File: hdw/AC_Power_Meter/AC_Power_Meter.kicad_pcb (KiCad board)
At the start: 4 copper layers, 100 x 100 mm, 280 parts, among them J1001 USB_B_Mini, J1701 Ext_SW_Toggle, J201 HT_IN, J202 NEUT_IN, J203 EARTH_IN, J401 HT_OUT, J402 NEUT_OUT, J403 EARTH_OUT, J501 AUX_IN, J801 Prog, Q1501 BT139-600, Q501 DMP3099L-7, SW1702 MRESET, SW1703 SW_Toggle, U1001 LT6700-1-S6, U1002 FT234XD, U1003 74LVC1G06, U1004 TPD3S014DBVR, U1101 ISO7321C, U1201 SSD1306, U1401 LTV-356T, U1402 74LVC1G17, U1501 74LVC1G32, U1502 FOD4218, U1601 74LVC1G06, U1602 74LVC1G06, U1603 74LVC1G06, U1604 74LVC1G06, U1605 74LVC1G06, U1606 74LVC1G06, U1607 74LVC1G06, U1702 TLC555CPS, U301 ACS722LLCTR-20AB, U501 LT6700-1-S6, U502 74LVC1G17, U601 74LVC1G17, U602 LT3973-DD, U701 PIC18LF67K40-I/PT, U801 TL331, U802 74LVC1G86, U901 LTC6240IS5, U902 LTC6240IS5, U903 LTC6240IS5, U904 LTC6240IS5, X701 ASV-16.000MHz

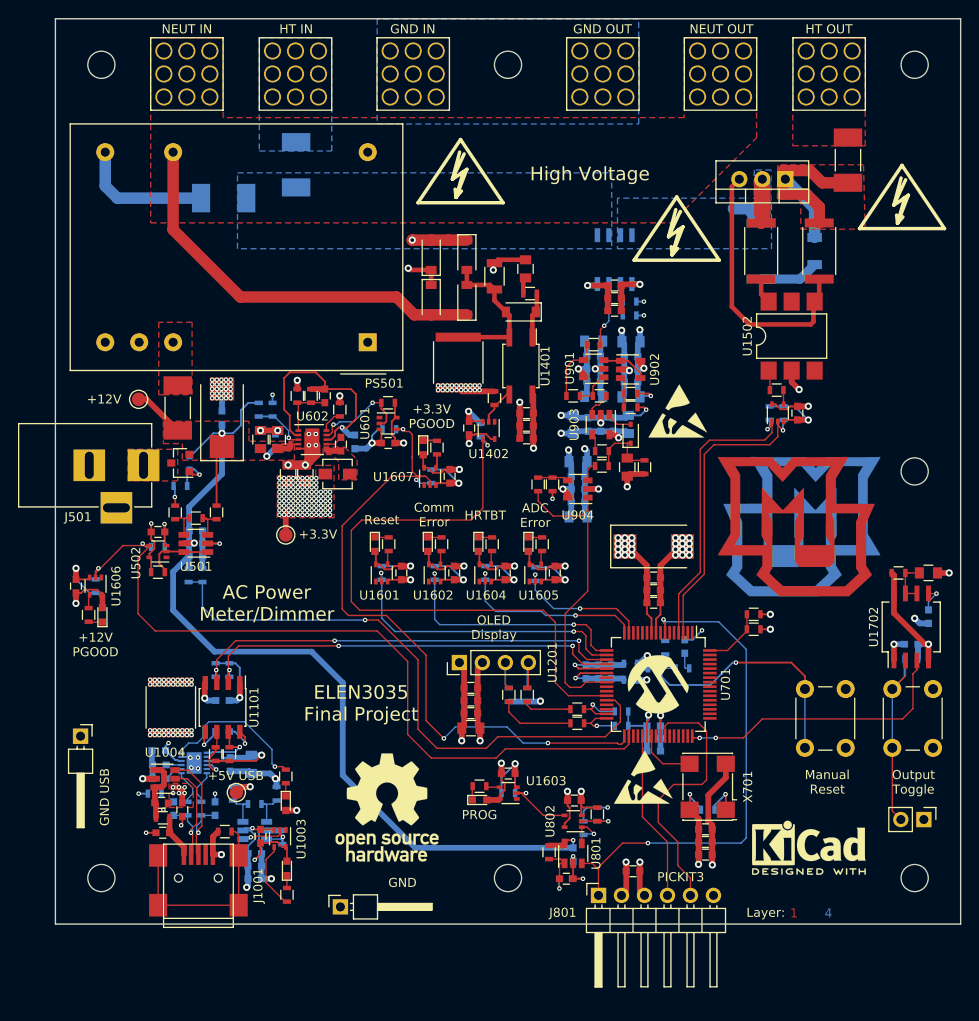
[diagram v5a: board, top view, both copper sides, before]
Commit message: Serious BOM scrubbing to drive price down
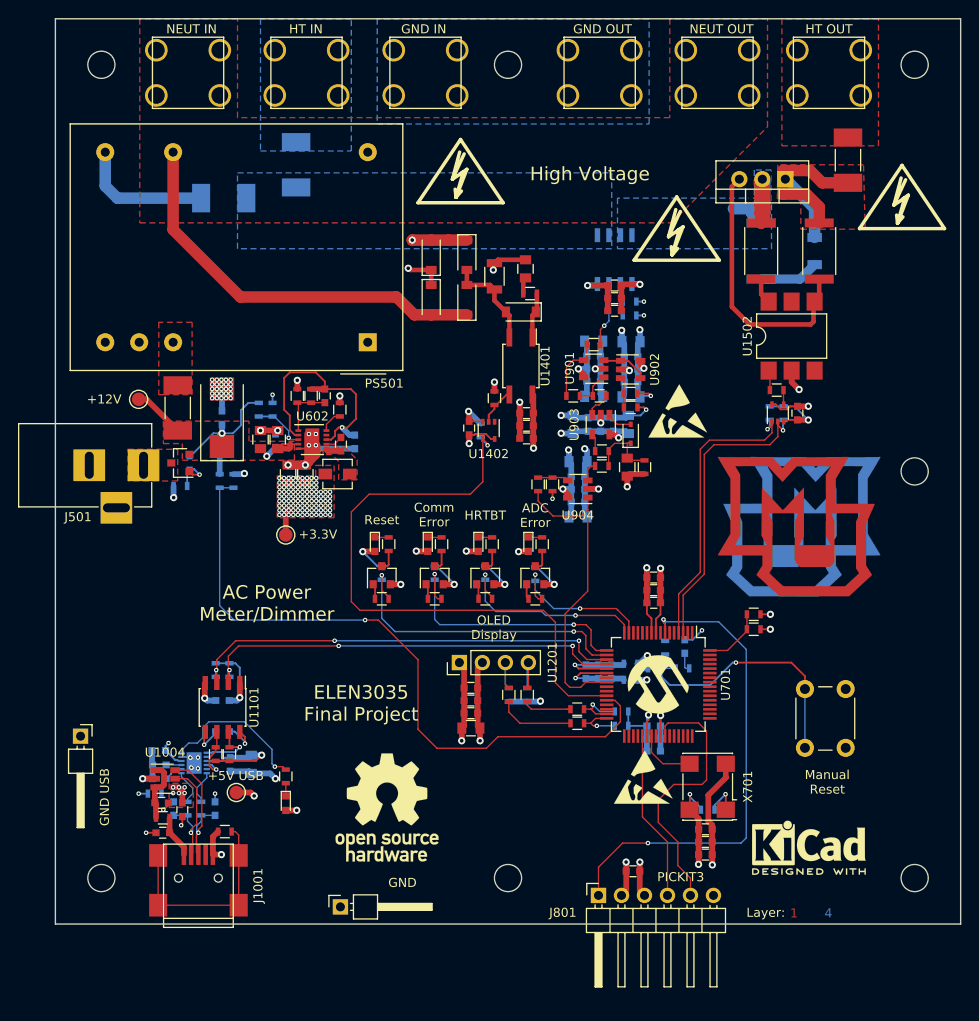
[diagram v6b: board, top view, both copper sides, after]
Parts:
- removed C1001, C1007, C1601, C1602, C1603, C1604, C1605, C1606, C1607, C1704, C501, C506, C602, C801, C802, C806: 0.1uF, Capacitors_SMD:C_0603
- removed C1002, C1702, C502: 10nF, Capacitors_SMD:C_0603
- removed C1003, C503: 1nF, Capacitors_SMD:C_0603
- removed C1102, C1402: 0.056uF, Capacitors_SMD:C_2220
- removed C1706: 1uF, Capacitors_SMD:C_0805
- removed C707: 47uF, Capacitors_Tantalum_SMD:CP_Tantalum_Case-X_EIA-7343-43_Reflow
- removed D1001, D1606, D1607: Green, LEDs:LED_0603
- removed D1603: Red, LEDs:LED_0603
- removed J1701: Ext_SW_Toggle, Pin_Headers:Pin_Header_Straight_1x02_Pitch2.54mm
- removed R1001: 487k, Resistors_SMD:R_0603
- removed R1002: 6.04k, Resistors_SMD:R_0603
- removed R1003: 40.2k, Resistors_SMD:R_0603
- removed R1005, R1605, R1610, R1613, R1702, R506, R507, R601, R604, R801, R802, R803: 10k, Resistors_SMD:R_0603
- removed R1006, R1607, R1612, R1614: 1k, Resistors_SMD:R_0603
- removed R1704: 100k, Resistors_SMD:R_0603
- removed R503: 1.4M, Resistors_SMD:R_0603
- removed R504: 10.5k, Resistors_SMD:R_0603
- removed R505: 43.2k, Resistors_SMD:R_0603
- removed R804: 0, Resistors_SMD:R_0603
- removed SW1703: SW_Toggle, Buttons_Switches_THT:SW_PUSH_6mm
- removed U1001, U501: LT6700-1-S6, TO_SOT_Packages_SMD:TSOT-23-6
- removed U1003, U1601, U1602, U1603, U1604, U1605, U1606, U1607: 74LVC1G06, TO_SOT_Packages_SMD:SOT-353_SC-70-5
- removed U1702: TLC555CPS, Housings_SOIC:SO-8_5.3x6.2mm_Pitch1.27mm
- removed U502, U601: 74LVC1G17, TO_SOT_Packages_SMD:SOT-353_SC-70-5
- removed U801: TL331, TO_SOT_Packages_SMD:SOT-23-5
- removed U802: 74LVC1G86, TO_SOT_Packages_SMD:SOT-353_SC-70-5
- removed Z801: UDZSTE-175.1B, Diodes_SMD:D_SOD-523
- added Q1401: 2N7002, TO_SOT_Packages_SMD:SOT-23, F.Cu at (107.7, 112.6)
- added Q1402: 2N7002, TO_SOT_Packages_SMD:SOT-23, F.Cu at (113.5, 112.6)
- added Q1403: 2N7002, TO_SOT_Packages_SMD:SOT-23, F.Cu at (119.1, 112.6)
- added Q1404: 2N7002, TO_SOT_Packages_SMD:SOT-23, F.Cu at (124.7, 112.6)
- added R1405: 10, Resistors_SMD:R_0603, F.Cu at (107.7, 115.3)
- added R1406: 10, Resistors_SMD:R_0603, F.Cu at (113.5, 115.3)
- added R1407: 10, Resistors_SMD:R_0603, F.Cu at (119.1, 115.3)
- added R1408: 10, Resistors_SMD:R_0603, F.Cu at (124.7, 115.3)
- J201, J202, J203, J401, J402, J403: footprint Custom Footprints Library:Wuerth_7461096_M4_Shank_9pos -> Custom Footprints Library:Keystone_8191
- moved R501 11.0 mm to (89.8, 102.2)
- moved R502 11.0 mm to (91.3, 102.2)
- moved J203 1.36 mm to (112.5, 57.1), turned to 90 degrees
- moved J201 1.22 mm to (99.4, 57.1), turned to 90 degrees
- moved J403 0.38 mm to (131.8, 57.1), turned to 90 degrees
- moved J402 0.36 mm to (144.8, 57.1), turned to 90 degrees
- moved J202 0.18 mm to (86.3, 57.1), turned to 90 degrees
- moved J401 0.13 mm to (157.1, 57.1), turned to 90 degrees
- renumbered SW1702 to SW801
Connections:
- U602 pad 9: Net-(R604-Pad2) -> (no net)
- U701 pad 33: POS3P3_PGOOD -> (no net)
- U701 pad 34: POS12_PGOOD -> (no net)
- U701 pad 48: SW_Toggle -> (no net)
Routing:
- net +12V: track 121.4 -> 28.9 mm, vias 4 -> 2
- net POS12_PGOOD: track 87.2 -> 0.00 mm, vias 2 -> 0
- net POS3P3_PGOOD: track 76.2 -> 0.00 mm, vias 4 -> 0
- net +3V3: track 230.7 -> 157.5 mm, vias 146 -> 127
- net GND: track 219.9 -> 154.0 mm, vias 129 -> 68
- net SW_Toggle: track 31.3 -> 0.00 mm, vias 2 -> 0
- net Net-(J1701-Pad2): track 22.4 -> 0.00 mm
- net +5V_USB: track 43.6 -> 25.1 mm, vias 14 -> 12
- net GND_USB: track 37.0 -> 24.7 mm, vias 34 -> 12
- net Net-(R604-Pad2): track 11.1 -> 0.00 mm, vias 2 -> 0
- net Net-(R1005-Pad2): track 8.74 -> 0.00 mm, vias 2 -> 0
- net ICSP_DETECT: track 8.53 -> 0.00 mm, vias 1 -> 0
- net POS12_ADC: track 66.1 -> 74.6 mm
- net Net-(R506-Pad2): track 7.75 -> 0.00 mm
- net Net-(R1006-Pad2): track 7.48 -> 0.00 mm
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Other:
- board text removed: "+12V PGOOD"
- board text removed: "+3.3V PGOOD"
- board text removed: "Output Toggle"
- board text removed: "PROG"

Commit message: Finished up PCB
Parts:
- added REF**: Symbol_Barrel_Polarity, Symbols:Symbol_Barrel_Polarity, F.Cu at (77.4, 109.1)
- moved REF*** 31.6 mm to (123.8, 137.1)
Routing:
- net ISNS_ADC: track 34.1 -> 34.9 mm
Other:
- board text added: "+"
- board text added: "-"
